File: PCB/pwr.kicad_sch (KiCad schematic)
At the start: 21 parts, among them J1 UJ2-MIBH2-4-SMT-TR, J5 Conn_01x02, J6 Conn_01x02, Q1 AO3401A, U2 LTC4412xS6, U3 USBLC6-2P6, U4 TPS62172DSG

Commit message: Production files
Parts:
- removed J1: UJ2-MIBH2-4-SMT-TR, UJ2-MIBH2-4-SMT-TR:CUI_UJ2-MIBH2-4-SMT-TR, symbol UJ2-MIBH2-4-SMT-TR:UJ2-MIBH2-4-SMT-TR
- added J1: USB_B_Micro, Connector_USB:USB_Micro-B_Molex-105017-0001, symbol Connector:USB_B_Micro
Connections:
- net D+: now also J1.3 (D+)
- net D-: now also J1.2 (D-)
- net GND: now also J1.5 (GND), J1.6 (Shield)
- net VBUS: now also J1.1 (VBUS)

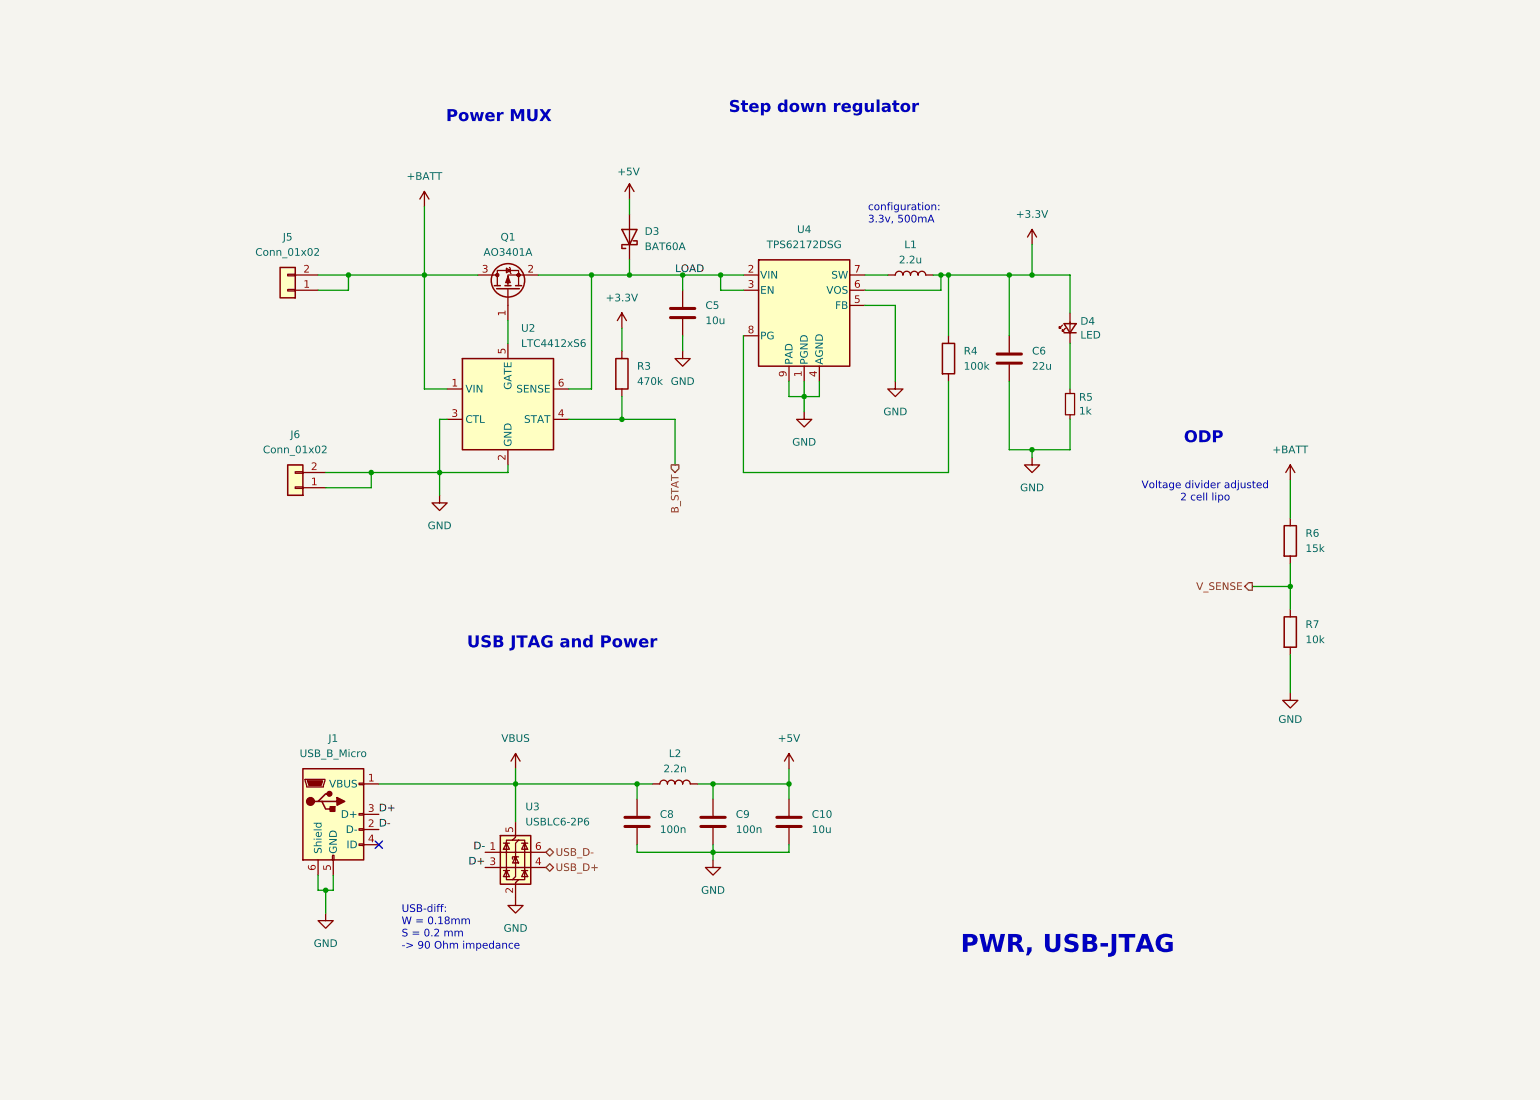
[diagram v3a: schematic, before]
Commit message: Started design of Inverter
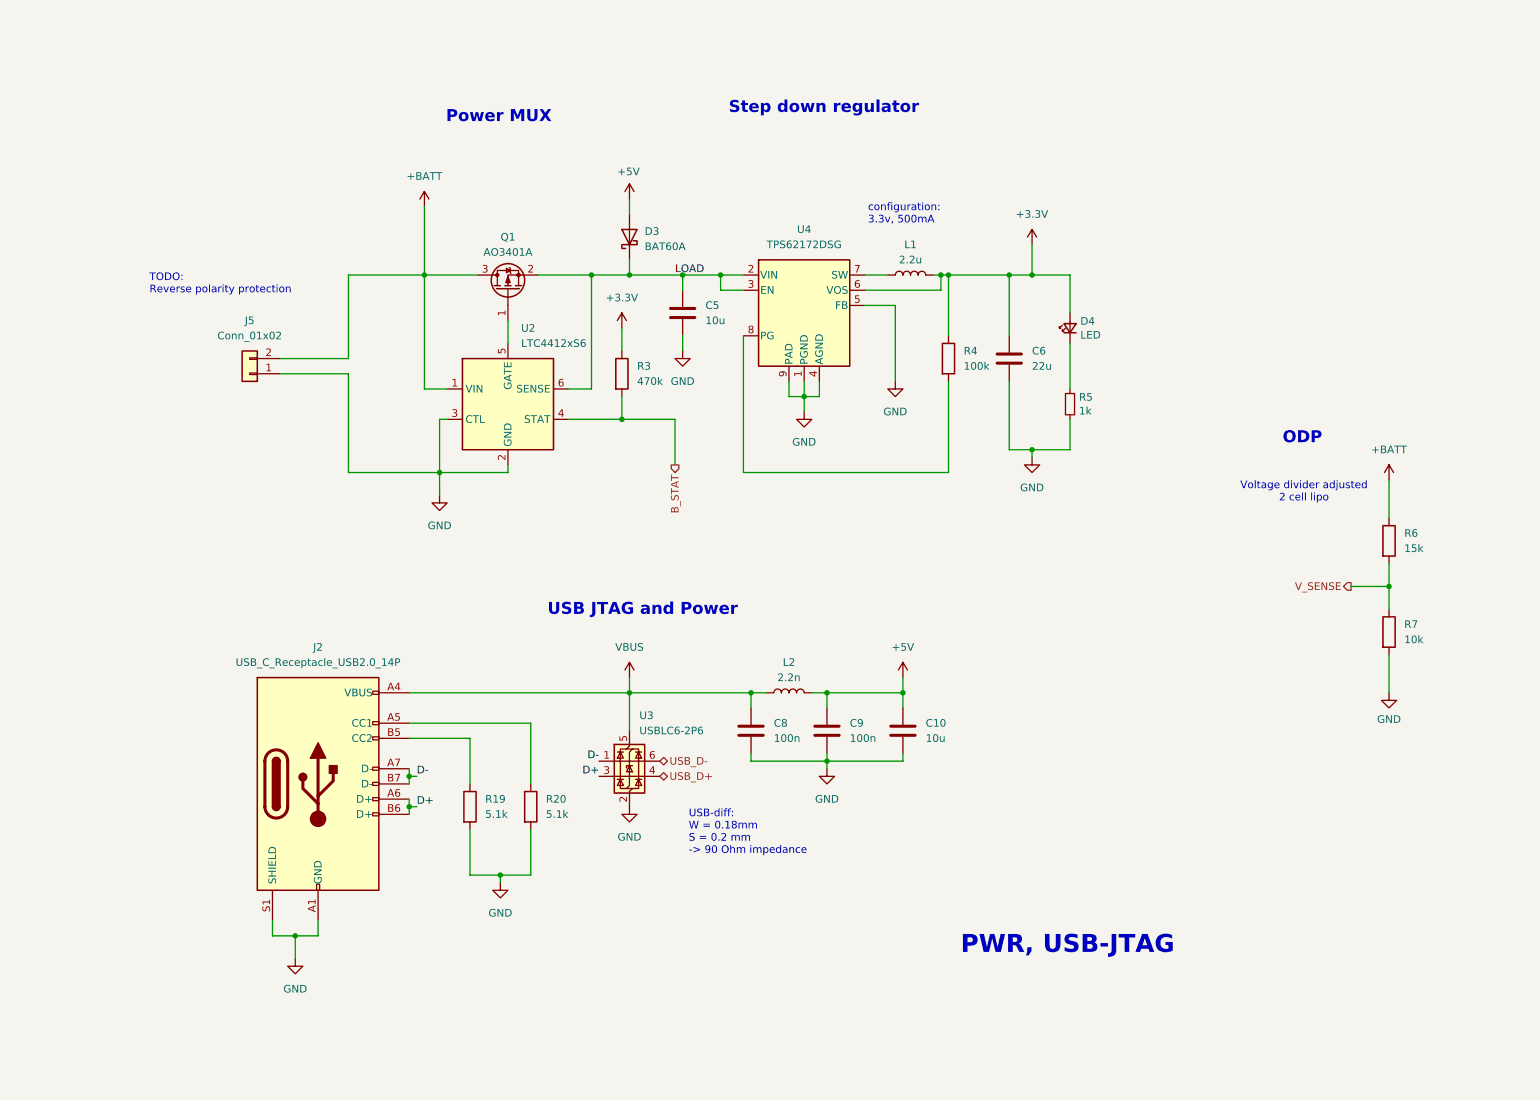
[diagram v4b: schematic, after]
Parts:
- removed J1: USB_B_Micro, Connector_USB:USB_Micro-B_Molex-105017-0001, symbol Connector:USB_B_Micro
- removed J6: Conn_01x02, Connector_PinHeader_2.54mm:PinHeader_1x02_P2.54mm_Vertical, symbol Connector_Generic:Conn_01x02
- added J2: USB_C_Receptacle_USB2.0_14P, Connector_USB:USB_C_Receptacle_G-Switch_GT-USB-7010ASV, symbol Connector:USB_C_Receptacle_USB2.0_14P
- added R19, R20: 5.1k, Resistor_SMD:R_0402_1005Metric, symbol Device:R
- J5: footprint Connector_PinHeader_2.54mm:PinHeader_1x02_P2.54mm_Vertical -> Connector_AMASS:AMASS_XT60-F_1x02_P7.20mm_Vertical
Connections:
- net +BATT: no longer J5.1 (Pin_1)
- net D+: now also J2.A6 (D+), J2.B6 (D+)
- net D-: now also J2.A7 (D-), J2.B7 (D-)
- net GND: now also J5.1 (Pin_1), J2.A1 (GND), J2.A12 (GND), J2.B1 (GND), J2.B12 (GND), J2.S1 (SHIELD), R19.2, R20.2
- net VBUS: now also J2.A4 (VBUS), J2.A9 (VBUS), J2.B4 (VBUS), J2.B9 (VBUS)
- new net: J2.A5 (CC1), R20.1
- new net: J2.B5 (CC2), R19.1
- no-connect marks 1 -> 0
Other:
- note added: "TODO: Reverse polarity protection"
- moved on the sheet: C10, C8, C9, J5, L2, R6, R7, U3

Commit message: Hardware updates: STM32H7 and Inverted design
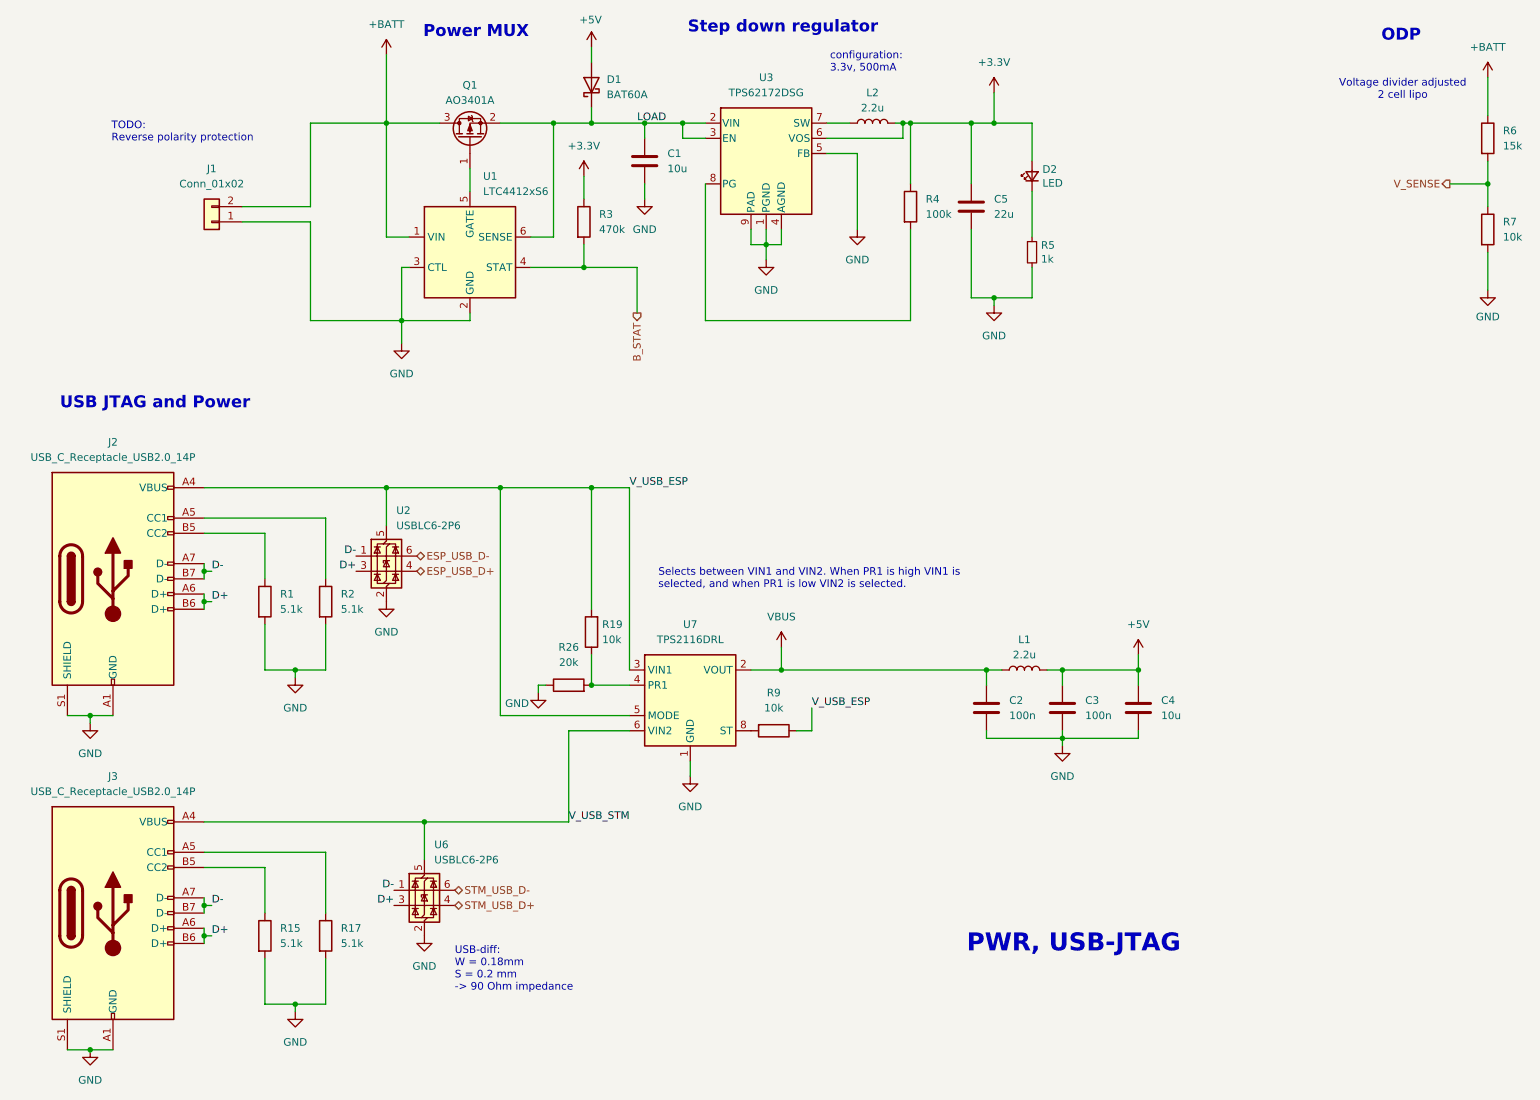
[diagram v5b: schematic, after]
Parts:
- added J3: USB_C_Receptacle_USB2.0_14P, Connector_USB:USB_C_Receptacle_G-Switch_GT-USB-7010ASV, symbol Connector:USB_C_Receptacle_USB2.0_14P
- added R15, R17: 5.1k, Resistor_SMD:R_0402_1005Metric, symbol Device:R
- added R19, R9: 10k, Resistor_SMD:R_0402_1005Metric, symbol Device:R
- added R26: 20k, Resistor_SMD:R_0402_1005Metric, symbol Device:R
- added U6: USBLC6-2P6, Package_TO_SOT_SMD:SOT-666, symbol Power_Protection:USBLC6-2P6
- added U7: TPS2116DRL, Package_TO_SOT_SMD:SOT-583-8, symbol Power_Management:TPS2116DRL
- L1: renamed from L2; value 2.2n -> 2.2u
- renumbered C5 to C1, C8 to C2, C9 to C3, C10 to C4, C6 to C5, D3 to D1, D4 to D2, J5 to J1, L1 to L2, R19 to R1, R20 to R2, U2 to U1, U3 to U2, U4 to U3
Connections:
- net D+: now also J3.A6 (D+), J3.B6 (D+), U6.3 (I/O2)
- net D-: now also J3.A7 (D-), J3.B7 (D-), U6.1 (I/O1)
- net GND: now also J3.A1 (GND), J3.A12 (GND), J3.B1 (GND), J3.B12 (GND), J3.S1 (SHIELD), R15.2, R17.2, R26.1, U6.2 (GND), U7.1 (GND)
- net VBUS: now also U7.2 (VOUT), U7.7 (VOUT); no longer J2.A4 (VBUS), J2.A9 (VBUS), J2.B4 (VBUS), J2.B9 (VBUS), U2.5 (VBUS)
- net USB_D+ renamed ESP_USB_D+
- net USB_D- renamed ESP_USB_D-
- new net: J3.A5 (CC1), R17.1
- new net: J3.B5 (CC2), R15.1
- new net: R19.1, R26.2, U7.4 (PR1)
- new net: R9.2, U7.8 (ST)
- new net STM_USB_D+: U6.4 (I/O2)
- new net STM_USB_D-: U6.6 (I/O1)
- new net V_USB_ESP: J2.A4 (VBUS), J2.A9 (VBUS), J2.B4 (VBUS), J2.B9 (VBUS), R19.2, R9.1, U2.5 (VBUS), U7.3 (VIN1), U7.5 (MODE)
- new net V_USB_STM: J3.A4 (VBUS), J3.A9 (VBUS), J3.B4 (VBUS), J3.B9 (VBUS), U6.5 (VBUS), U7.6 (VIN2)
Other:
- note added: "Selects between VIN1 and VIN2. When PR1 is high VIN1 is selected, and when PR1 is low VIN2 is selected."
- moved on the sheet: C1, C2, C3, C4, C5, D1, D2, J1, J2, L1, L2, Q1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
